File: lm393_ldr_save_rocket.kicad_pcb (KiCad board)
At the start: 2 copper layers, 35 x 74 mm, 17 parts, among them J1 BAT 9V, J2 IGNITER, M3 M3, Q1 TIP122, U1 LM7805, U2 LM393

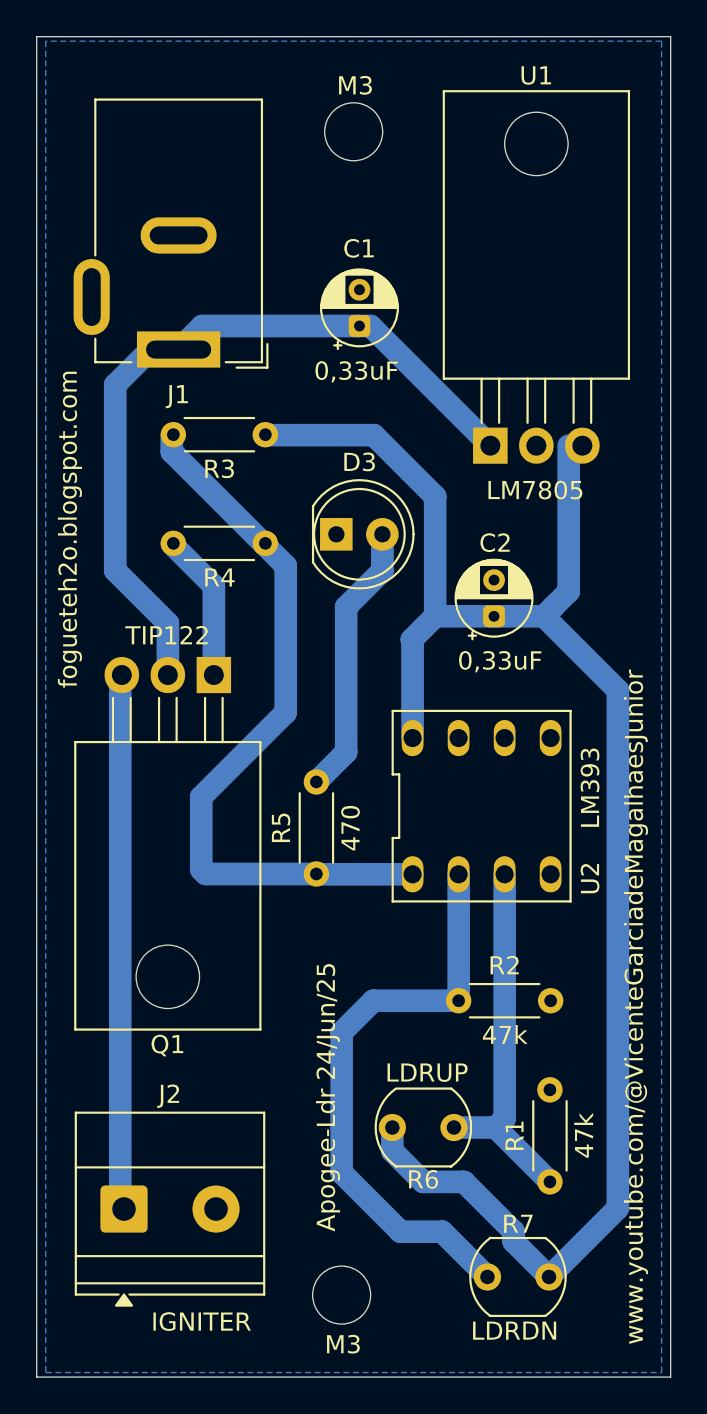
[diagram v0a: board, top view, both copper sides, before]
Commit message: ajustes de posicionamento de componentes na placa
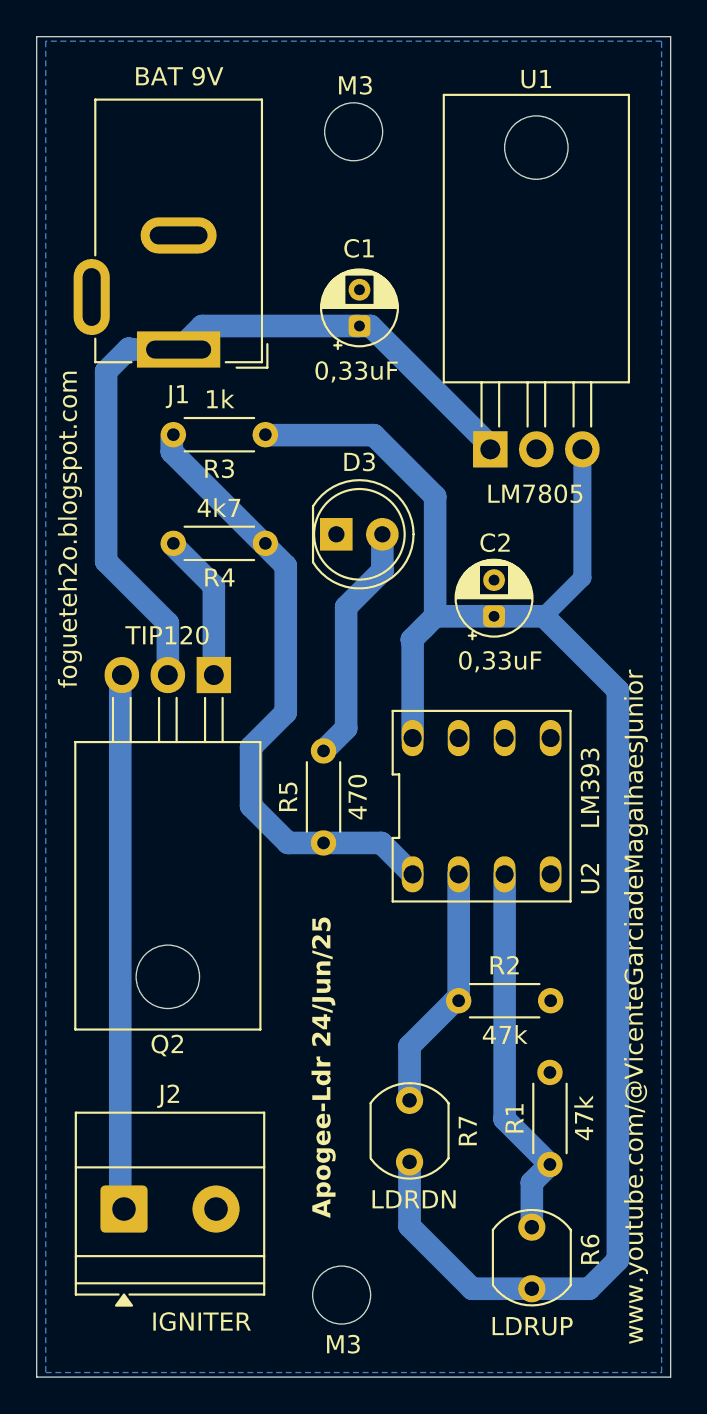
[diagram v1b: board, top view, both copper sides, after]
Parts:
- Q2: renamed from Q1; value TIP122 -> TIP120
- moved R7 10.7 mm to (105.5, 122.2), turned to -90 degrees
- moved R6 6.98 mm to (112.2, 129.2), turned to -90 degrees
- moved R5 1.76 mm to (100.8, 108.0)
- moved R1 0.96 mm to (113.2, 125.8)
- moved U1 0.20 mm to (110.0, 86.3)
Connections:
- R4 pad 2: Net-(Q1-B) -> Net-(Q2-B)
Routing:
- net Net-(U2A--): track 32.3 -> 13.7 mm
- net Net-(R3-Pad2): track 40.3 -> 34.3 mm
- net Net-(D3-A): track 15.2 -> 13.3 mm
- net /VCC: track 93.6 -> 95.2 mm
- net Net-(J1-Pin_1): track 42.3 -> 43.4 mm

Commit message: jumper de segurança
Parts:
- added J3: JUMP, Button_Switch_THT:SW_DIP_SPSTx01_Slide_6.7x4.1mm_W7.62mm_P2.54mm_LowProfile, F.Cu at (101.7, 111.7)
- moved Q2 0.24 mm to (94.5, 98.6)
- moved C1 0.23 mm to (102.5, 79.5)
- moved C2 0.09 mm to (110.2, 95.5)
- moved U1 0.06 mm to (110.0, 86.2)
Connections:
- Q2 pad 1: Net-(Q1-B) -> Net-(Q2-B)
- Q2 pad 3: Net-(J2-Pin_1) -> Net-(J3-Pin_1)
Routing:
- net Net-(J3-Pin_1): track 0.00 -> 22.0 mm
- net Net-(J2-Pin_1): track 29.6 -> 18.4 mm
- net Net-(Q2-B): track 0.00 -> 8.20 mm
- net Net-(Q1-B): track 8.20 -> 0.00 mm

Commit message: basicamente update de backup
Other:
- board text added: "Apogee-Ldr Jun/25"
- board text removed: "Apogee-Ldr 24/Jun/25"
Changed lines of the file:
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@@
 		(layer "Edge.Cuts")
 	)
-	(gr_text "Apogee-Ldr 24/Jun/25"
+	(gr_text "Apogee-Ldr Jun/25"
 		(at 118.5 94.25 90)
 		(layer "F.SilkS")

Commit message: novo tamanho 5x5 cm
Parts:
- moved M3 106.7 mm to (179.5, 142.5)
- moved M3 58.4 mm to (159.0, 144.5)
- moved J2 42.2 mm to (124.9, 105.0)
- moved Q2 41.6 mm to (130.3, 77.3)
- moved C2 25.7 mm to (104.5, 70.5)
- moved C1 25.6 mm to (126.5, 70.5)
- moved J3 24.7 mm to (117.5, 92.7)
- moved R1 22.5 mm to (106.0, 104.5), turned to -90 degrees
- moved R6 20.6 mm to (118.0, 109.5), turned to 90 degrees
- moved R7 20.4 mm to (110.0, 102.4), turned to 90 degrees
- moved U1 18.9 mm to (116.5, 68.5), turned to 180 degrees
- moved D3 16.9 mm to (96.0, 107.0), turned to 180 degrees
- moved U2 16.3 mm to (98.2, 94.3)
- moved R2 14.5 mm to (100.5, 104.5), turned to -90 degrees
- moved R5 12.3 mm to (89.0, 104.5), turned to -90 degrees
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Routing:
- net Net-(Q2-B): track 8.20 -> 32.9 mm
- net /VCC: track 95.2 -> 73.1 mm
- net Net-(J1-Pin_1): track 43.4 -> 59.2 mm
- net Net-(U2A--): track 13.7 -> 25.2 mm
- net Net-(J2-Pin_1): track 18.4 -> 9.37 mm
- net Net-(D3-A): track 13.3 -> 5.53 mm
- net Net-(U2A-+): track 20.9 -> 24.6 mm
- net Net-(J3-Pin_1): track 22.0 -> 18.5 mm
- net Net-(R3-Pad2): track 34.3 -> 33.0 mm
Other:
- board size 35 x 74 mm -> 50 x 50 mm

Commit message: posicionamento carga tip120
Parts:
- R4: value 4k7 -> 470
- R5: value 470 -> 220
- moved M3 96.3 mm to (89.0, 109.5)
- moved M3 81.9 mm to (131.0, 67.5)
- moved Q2 18.0 mm to (125.0, 94.5), turned to 0 degrees
- moved R5 9.54 mm to (89.0, 95.0)
- moved C1 3.41 mm to (123.1, 70.6)
- moved D3 3.16 mm to (95.0, 104.0)
- moved U2 2.50 mm to (98.2, 91.8)
- moved R3 1.00 mm to (90.0, 85.5)
- moved R6 1.00 mm to (117.0, 109.5)
- moved C2 0.15 mm to (104.6, 70.6)
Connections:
- J2 pad 2: /GND -> Net-(J2-Pin_2)
- J3 pad 1: Net-(J3-Pin_1) -> Net-(J1-Pin_1)
- Q2 pad 2: Net-(J1-Pin_1) -> Net-(J2-Pin_2)
- Q2 pad 3: Net-(J3-Pin_1) -> /GND
- R5 pad 1: Net-(R3-Pad2) -> /VCC
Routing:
- net Net-(J3-Pin_1): track 18.5 -> 0.00 mm
- net Net-(Q2-B): track 32.9 -> 16.7 mm
- net Net-(J2-Pin_2): track 0.00 -> 11.5 mm
- net Net-(J1-Pin_1): track 59.2 -> 68.8 mm
- net /VCC: track 73.1 -> 80.6 mm
- net Net-(R3-Pad2): track 33.0 -> 25.6 mm
- net Net-(U2A--): track 25.2 -> 31.3 mm
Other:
- board text added: "Apogee-Ldr"
- board text added: "FogueteH2O Jun/25"
- board text removed: "Apogee-Ldr Jun/25"

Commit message: finalizada com order para JCLPCB
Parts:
- removed D3: LED, LED_THT:LED_D5.0mm
- removed M3 (x2): M3, MountingHole:MountingHole_3.2mm_M3
- added D1: LED, LED_THT:LED_D5.0mm, F.Cu at (106.7, 67.3)
- added J4: ON-OFF, Button_Switch_THT:SW_DIP_SPSTx01_Slide_6.7x4.1mm_W7.62mm_P2.54mm_LowProfile, F.Cu at (95.9, 91.0)
- added Q1: BC548, Package_TO_SOT_THT:TO-92L_Inline_Wide, F.Cu at (93.9, 79.8)
- added R8: 220, Resistor_THT:R_Axial_DIN0204_L3.6mm_D1.6mm_P5.08mm_Horizontal, F.Cu at (113.1, 79.8)
- J2: value IGNITER -> TRIGGER
- J3: value JUMP -> READY
- R5: value 220 -> 470
- R6, R7: footprint OptoDevice:R_LDR_5.1x4.3mm_P3.4mm_Vertical -> Connector_PinHeader_2.54mm:PinHeader_1x02_P2.54mm_Vertical
- moved J2 44.9 mm to (99.0, 68.3), turned to 180 degrees
- moved C1 39.3 mm to (111.8, 108.3), turned to 180 degrees
- moved U1 36.0 mm to (116.0, 104.5), turned to -90 degrees
- moved R2 35.1 mm to (130.2, 85.8)
- moved C2 32.0 mm to (120.0, 98.6), turned to 180 degrees
- moved R7 30.8 mm to (130.2, 79.1), turned to 180 degrees
- moved R6 30.7 mm to (121.5, 79.1), turned to 180 degrees
- moved Q2 30.6 mm to (116.0, 65.3), turned to -90 degrees
- moved J1 28.4 mm to (105.7, 106.8), turned to -90 degrees
- moved R1 27.1 mm to (125.5, 85.8)
- moved R5 23.3 mm to (106.7, 79.8), turned to 90 degrees
- moved U2 17.7 mm to (115.7, 88.6)
- moved R3 15.5 mm to (105.5, 85.8)
- moved R4 10.3 mm to (99.0, 86.6), turned to 180 degrees
- moved J3 9.22 mm to (109.5, 97.4), turned to 180 degrees
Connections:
- C1 pad 1: Net-(J1-Pin_1) -> Net-(J3-Pin_1)
- J3 pad 1: Net-(J1-Pin_1) -> Net-(J3-Pin_1)
- R5 pad 1: /VCC -> Net-(R5-Pad1)
- U1 pad 1: Net-(J1-Pin_1) -> Net-(J3-Pin_1)
- U2 pad 5: (no net) -> Net-(U2A--)
- U2 pad 6: (no net) -> Net-(U2A-+)
- U2 pad 7: (no net) -> Net-(R5-Pad1)
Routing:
- net Net-(J1-Pin_1): track 68.8 -> 32.8 mm
- net Net-(J3-Pin_1): track 0.00 -> 32.9 mm
- net Net-(J2-Pin_1): track 9.37 -> 33.6 mm
- net Net-(R5-Pad1): track 0.00 -> 22.7 mm
- net Net-(Q2-B): track 16.7 -> 38.7 mm
- net Net-(D1-K): track 0.00 -> 21.1 mm
- net Net-(J2-Pin_2): track 11.5 -> 26.6 mm
- net Net-(R3-Pad2): track 25.6 -> 15.3 mm
- net Net-(D1-A): track 0.00 -> 9.47 mm
- net Net-(Q1-B): track 5.39 -> 13.3 mm
- net /VCC: track 80.6 -> 86.7 mm
- net Net-(U2A-+): track 24.7 -> 26.5 mm
- net Net-(U2A--): track 31.3 -> 30.6 mm
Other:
- board size 50 x 50 mm -> 48.7 x 54.3 mm
- board text added: "FogueteH2O"
- board text added: "FogueteH2O YouTube Jul/25"
- board text added: "Julho/2025"
- board text added: "vicente.gmj@gmail.com"
- board text removed: "Apogee-Ldr"
- board text removed: "FogueteH2O Jun/25"
- board text removed: "fogueteh2o.blogspot.com"
- board text removed: "www.youtube.com/@VicenteGarciadeMagalhaesJunior"
